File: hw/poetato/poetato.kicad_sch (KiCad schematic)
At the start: 16 parts, among them M1 Light pipe, M10 Jumper, M11 Face Plate 1, M12 Face Plate 1, M13 Face Plate 2, M14 Face Plate 3, M15 Phoenix 12P plug, M16 Phoenix 4P plug, M2 Light pipe, M3 Light pipe, M4 Light pipe, M5 Light pipe, M6 Light pipe, M7 Light pipe, M8 Light pipe, M9 Enclosure

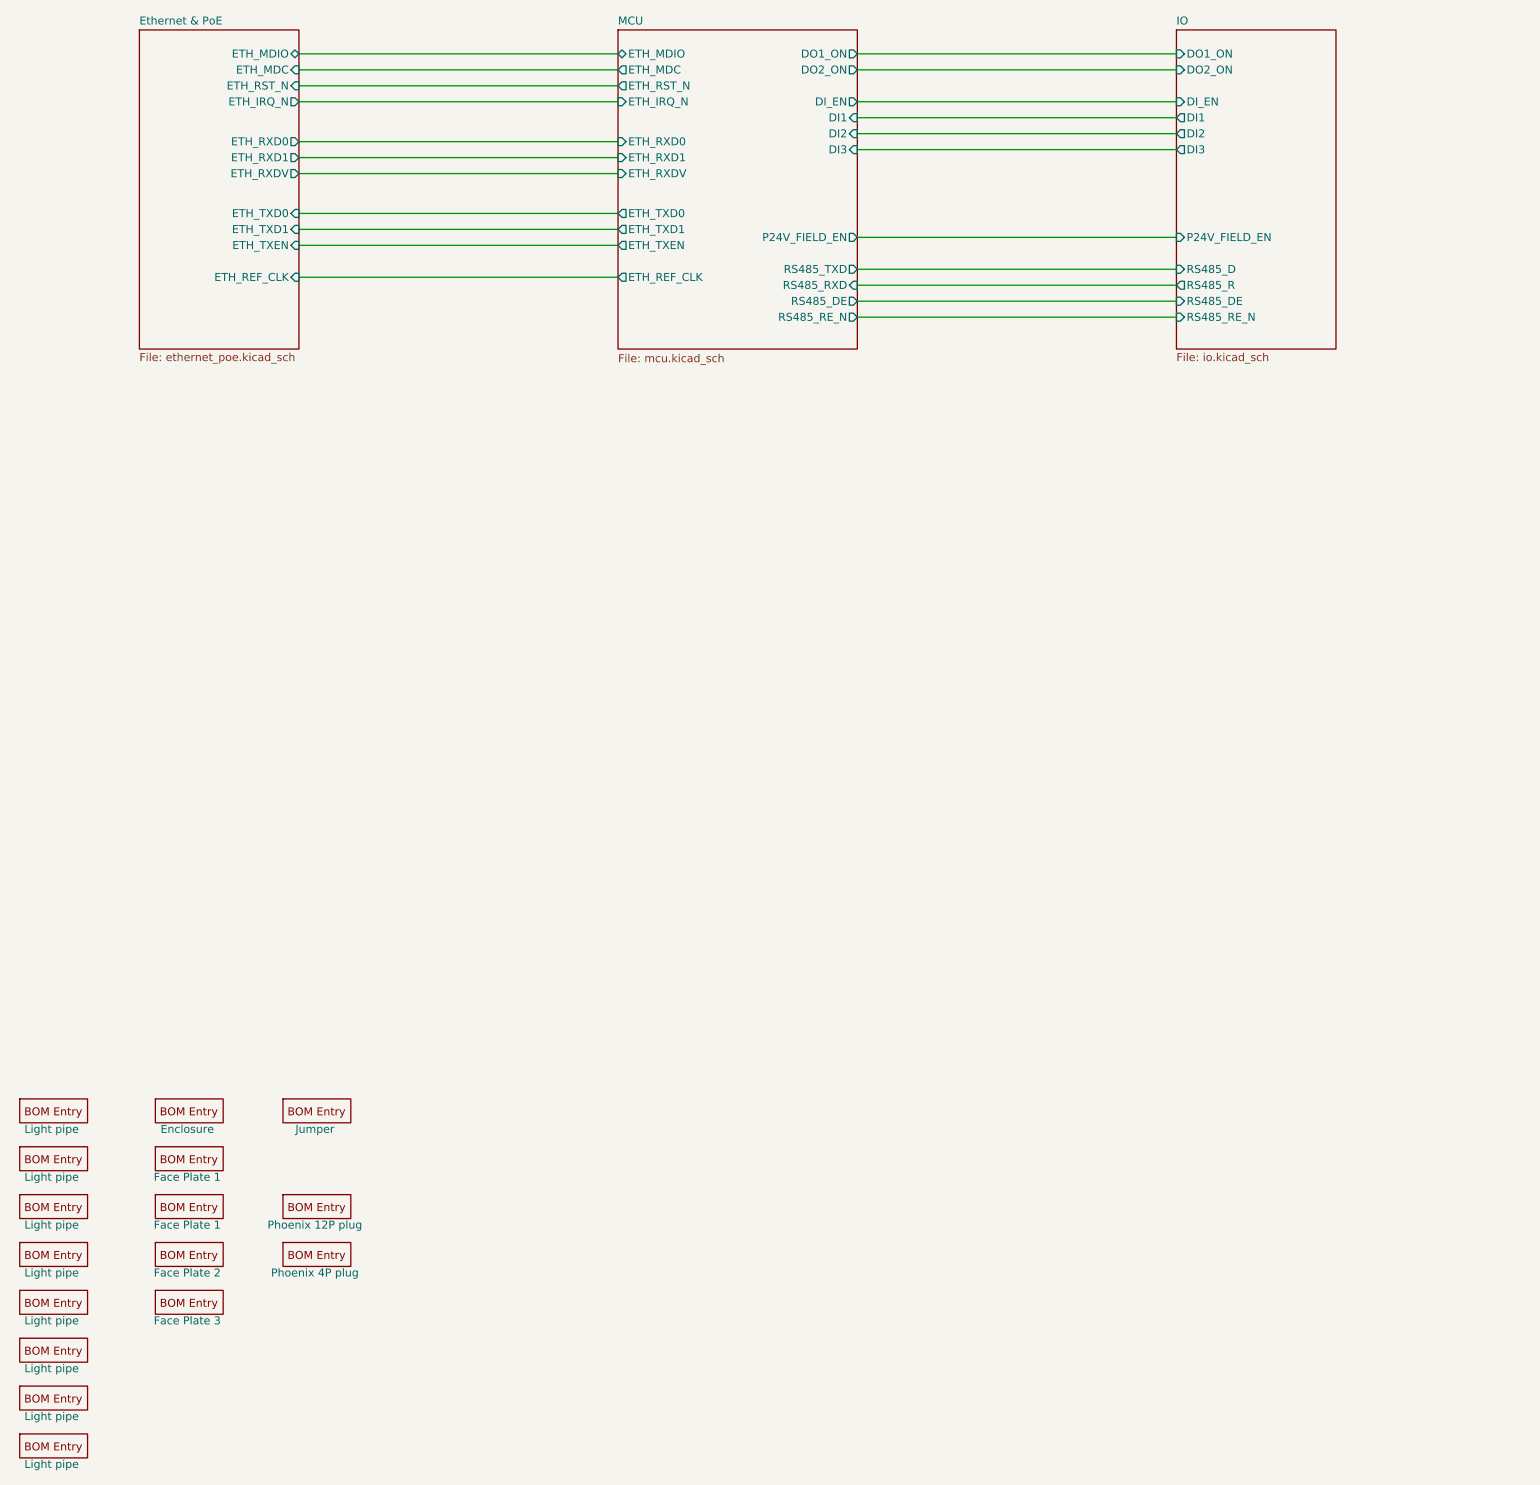
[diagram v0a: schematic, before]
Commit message: hw: add power tree to top-level sheet
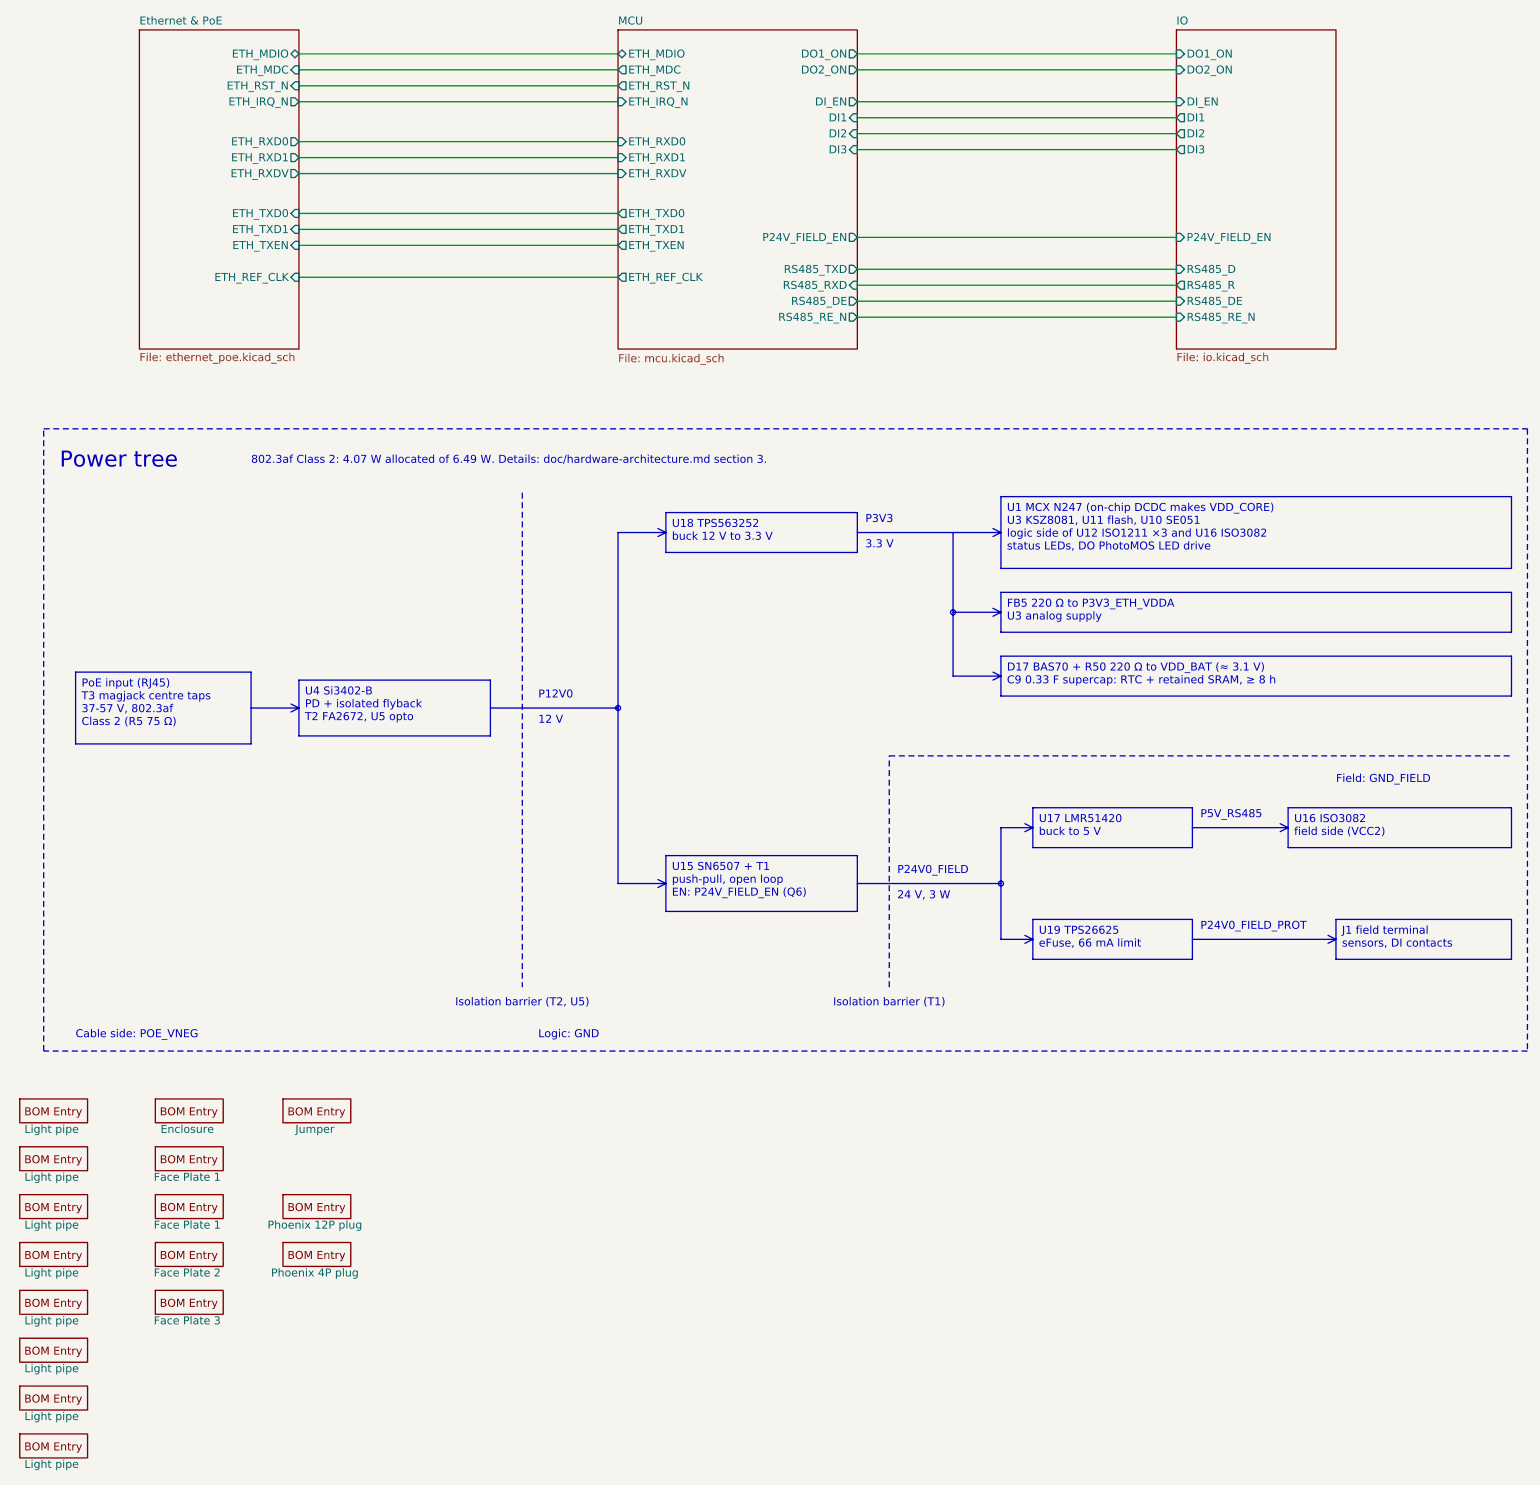
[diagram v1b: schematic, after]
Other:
- note added: "12 V"
- note added: "24 V, 3 W"
- note added: "3.3 V"
- note added: "802.3af Class 2: 4.07 W allocated of 6.49 W. Details: doc/hardware-architecture.md section 3."
- note added: "Cable side: POE_VNEG"
- note added: "Field: GND_FIELD"
- note added: "Isolation barrier (T1)"
- note added: "Isolation barrier (T2, U5)"
- note added: "Logic: GND"
- note added: "P12V0"
- note added: "P24V0_FIELD"
- note added: "P24V0_FIELD_PROT"
- note added: "P3V3"
- note added: "P5V_RS485"
- note added: "Power tree"

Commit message: hw: move the DC/DC converters to a new top-level Power sheet
power.kicad_sch (page 4) holds the 3.3 V buck (from MCU), the isolated
24 V field supply with its enable FET and LED (from IO) and the RS-485
5 V buck (from RS485). The two bucks are mirrored to read left to right.
The PoE flyback stays on the Ethernet sheet.

P5V_RS485 is now a power symbol and P24V_FIELD_EN goes from MCU to the
Power sheet at the top level. On IO the eFuse moved next to J1, removing
the output loop around the page. The power tree is redrawn more compact
to make room for the new sheet symbol.

Symbols keep their UUIDs and references. ERC clean; every net connects
the same pins as before, 7 nets renamed by the new sheet path.
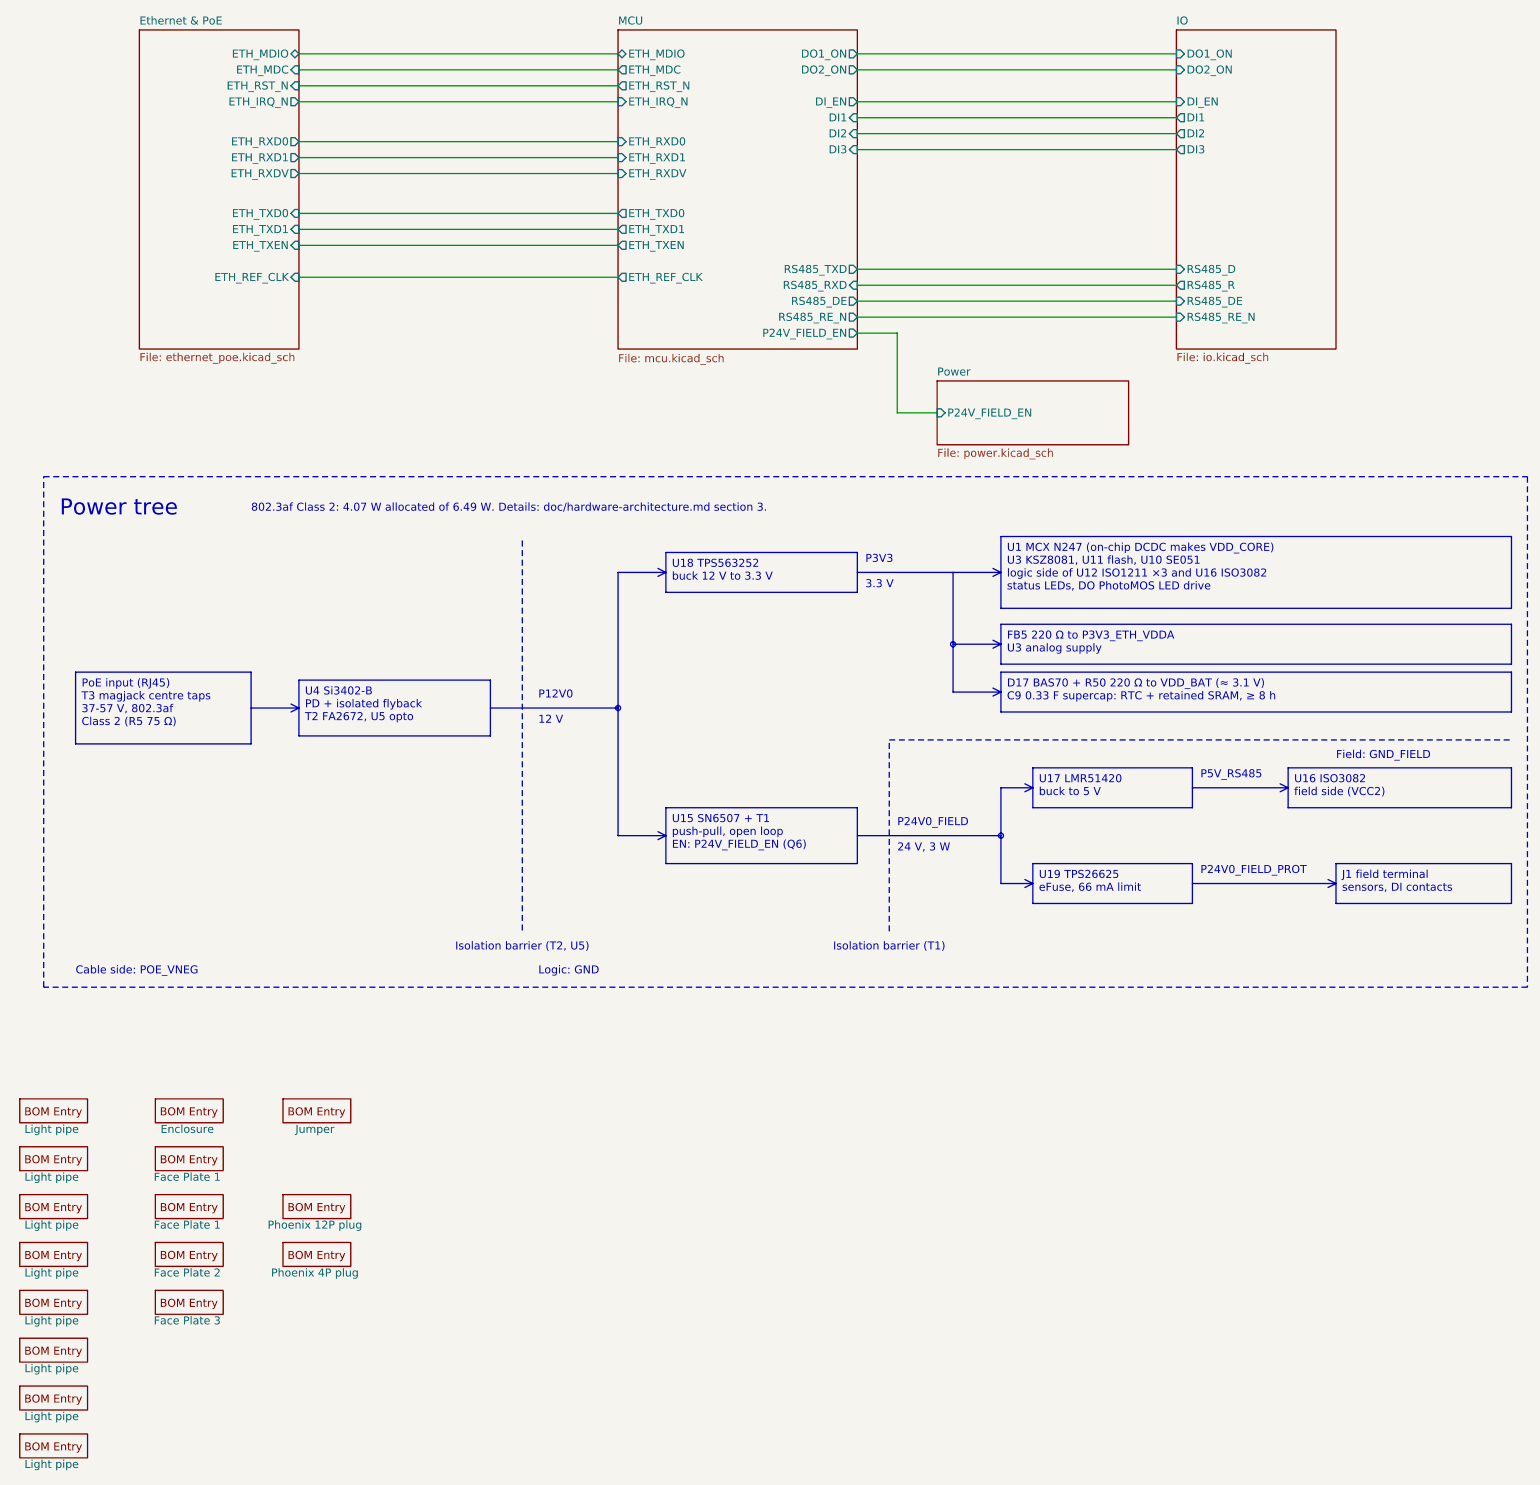
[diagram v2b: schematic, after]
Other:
- added sheet Power (power.kicad_sch)
- sheet IO ports: added none; removed P24V_FIELD_EN
